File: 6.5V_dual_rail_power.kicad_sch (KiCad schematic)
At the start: 12 parts, among them U2 TSR2-2465, U3 TSR2-2465

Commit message: Save progress.
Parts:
- F1, F2: footprint (none) -> Fuse:Fuse_Littelfuse-NANO2-451_453; DigiKey Part Number (none) -> F2602TR-ND; Manufacturer (none) -> Littelfuse Inc.; Manufacturer Part Number (none) -> 0452002.MRL; Package/Footprint (none) -> 2-SMD, Square End Block; Type (none) -> SMD
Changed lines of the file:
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@@
 			)
 		)
-		(property "Footprint" ""
+		(property "Footprint" "Fuse:Fuse_Littelfuse-NANO2-451_453"
 			(at 173.99 77.978 90)
 			(hide yes)
@@
 			)
 		)
-		(property "Datasheet" ""
-			(at 173.99 76.2 0)
-			(hide yes)
-			(show_name no)
-			(do_not_autoplace no)
-			(effects
-				(font
-					(size 1.27 1.27)
-				)
-			)
-		)
-		(property "Description" "Fuse"
+		(property "Datasheet" "https://www.littelfuse.com/assetdocs/littelfuse-fuse-452-454-datasheet?assetguid=8c87aa93-80a7-4ea8-8749-a19ba03901c2"
+			(at 173.99 76.2 0)
+			(hide yes)
+			(show_name no)
+			(do_not_autoplace no)
+			(effects
+				(font
+					(size 1.27 1.27)
+				)
+			)
+		)
+		(property "Description" "FUSE BRD MNT 2A 125VAC/VDC 2SMD"
+			(at 173.99 76.2 0)
+			(hide yes)
+			(show_name no)
+			(do_not_autoplace no)
+			(effects
+				(font
+					(size 1.27 1.27)
+				)
+			)
+		)
+		(property "Manufacturer" "Littelfuse Inc."
+			(at 173.99 76.2 0)
+			(hide yes)
+			(show_name no)
+			(do_not_autoplace no)
+			(effects
+				(font
+					(size 1.27 1.27)
+				)
+			)
+		)
+		(property "Manufacturer Part Number" "0452002.MRL"
+			(at 173.99 76.2 0)
+			(hide yes)
+			(show_name no)
+			(do_not_autoplace no)
+			(effects
+				(font
+					(size 1.27 1.27)
+				)
+			)
+		)
+		(property "DigiKey Part Number" "F2602TR-ND"
+			(at 173.99 76.2 0)
+			(hide yes)
+			(show_name no)
+			(do_not_autoplace no)
+			(effects
+				(font
+					(size 1.27 1.27)
+				)
+			)
+		)
+		(property "Type" "SMD"
+			(at 173.99 76.2 0)
+			(hide yes)
+			(show_name no)
+			(do_not_autoplace no)
+			(effects
+				(font
+					(size 1.27 1.27)
+				)
+			)
+		)
+		(property "Package/Footprint" "2-SMD, Square End Block"
 			(at 173.99 76.2 0)
 			(hide yes)
@@
 			)
 		)
-		(property "Footprint" ""
+		(property "Footprint" "Fuse:Fuse_Littelfuse-NANO2-451_453"
 			(at 173.99 103.378 90)
 			(hide yes)
@@
 			)
 		)
-		(property "Datasheet" ""
-			(at 173.99 101.6 0)
-			(hide yes)
-			(show_name no)
-			(do_not_autoplace no)
-			(effects
-				(font
-					(size 1.27 1.27)
-				)
-			)
-		)
-		(property "Description" "Fuse"
-			(at 173.99 101.6 0)
-			(hide yes)
+		(property "Datasheet" "https://www.littelfuse.com/assetdocs/littelfuse-fuse-452-454-datasheet?assetguid=8c87aa93-80a7-4ea8-8749-a19ba03901c2"
+			(at 173.99 101.6 0)
+			(hide yes)
+			(show_name no)
+			(do_not_autoplace no)
+			(effects
+				(font
+					(size 1.27 1.27)
+				)
+			)
+		)
+		(property "Description" "FUSE BRD MNT 2A 125VAC/VDC 2SMD"
+			(at 173.99 101.6 0)
+			(hide yes)
+			(show_name no)
+			(do_not_autoplace no)
+			(effects
+				(font
+					(size 1.27 1.27)
+				)
+			)
+		)
+		(property "Manufacturer" "Littelfuse Inc."
+			(at 173.99 101.6 0)
+			(hide yes)
+			(show_name no)
+			(do_not_autoplace no)
+			(effects
+				(font
+					(size 1.27 1.27)
+				)
+			)
+		)
+		(property "Manufacturer Part Number" "0452002.MRL"
+			(at 173.99 101.6 0)
+			(hide yes)
+			(show_name no)
+			(do_not_autoplace no)
+			(effects
+				(font
+					(size 1.27 1.27)
+				)
+			)
+		)
+		(property "DigiKey Part Number" "F2602TR-ND"
+			(at 173.99 101.6 0)
+			(hide yes)
+			(show_name no)
+			(do_not_autoplace no)
+			(effects
+				(font
+					(size 1.27 1.27)
+				)
+			)
+		)
+		(property "Type" "SMD"
+			(at 173.99 101.6 0)
+			(hide yes)
+			(show_name no)
+			(do_not_autoplace no)
+			(effects
+				(font
+					(size 1.27 1.27)
+				)
+			)
+		)
+		(property "Package/Footprint" "2-SMD, Square End Block"
+			(at 173.99 101.6 0)
+			(hide yes)

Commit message: Save progress.
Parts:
- added C10, C11, C12, C9: 10uF, Capacitor_SMD:C_1206_3216Metric_Pad1.33x1.80mm_HandSolder, symbol DK_Murata_GRM_1206_Capacitors:C_10uF
- added L1, L2: 5.6uH, 1_L_SMD:TCK141, symbol 1_L_SMD:TCK-141
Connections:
- net +15V: now also C10.1, C9.1, L1.1; no longer C5.1, C6.1, U2.1 (Vin)
- net -15V: now also C11.2, C12.2, L2.2; no longer C7.2, C8.2, U3.2 (GND)
- net GND: now also C10.2, C11.1, C12.1, C9.2
- new net: C7.2, C8.2, L2.1, U3.2 (GND)
- new net: C5.1, C6.1, L1.2, U2.1 (Vin)

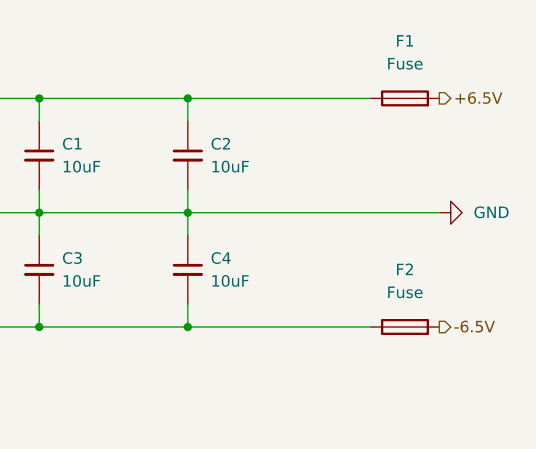
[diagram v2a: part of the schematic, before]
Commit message: Exchange SMD fuse with SMD fuse holder.
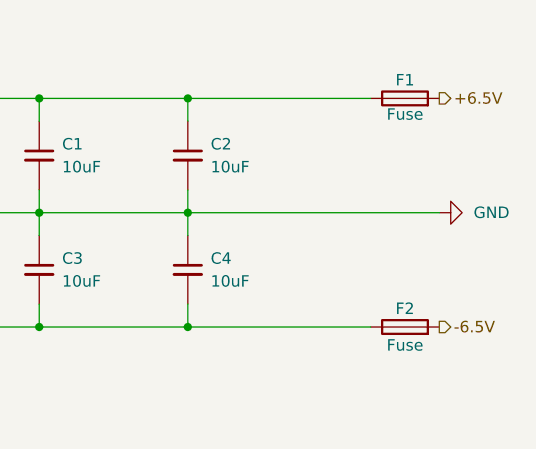
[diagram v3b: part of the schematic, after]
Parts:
- removed F1, F2: Fuse, Fuse:Fuse_Littelfuse-NANO2-451_453, symbol Device:Fuse
- added F1, F2: Fuse, 1_Fuse_SMD:LittleFuse_01550900M, symbol 1_Fuse_SMD:Littlefuse OMNI-BLOK Holder
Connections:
- net +6.5V: now also F1.2
- net -6.5V: now also F2.2
- net at C1.1, C2.1, U2.3 (Vout): now also F1.1
- net at C3.2, C4.2, U3.3 (Vout): now also F2.1

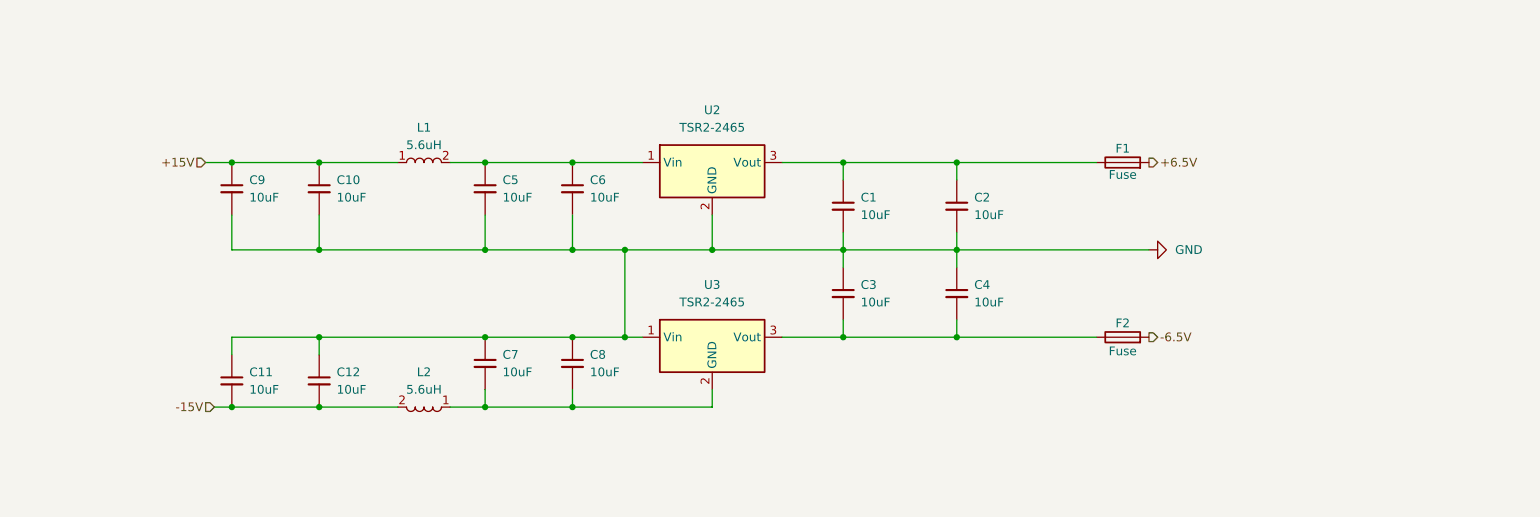
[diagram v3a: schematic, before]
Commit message: Added and routed power LEDs.
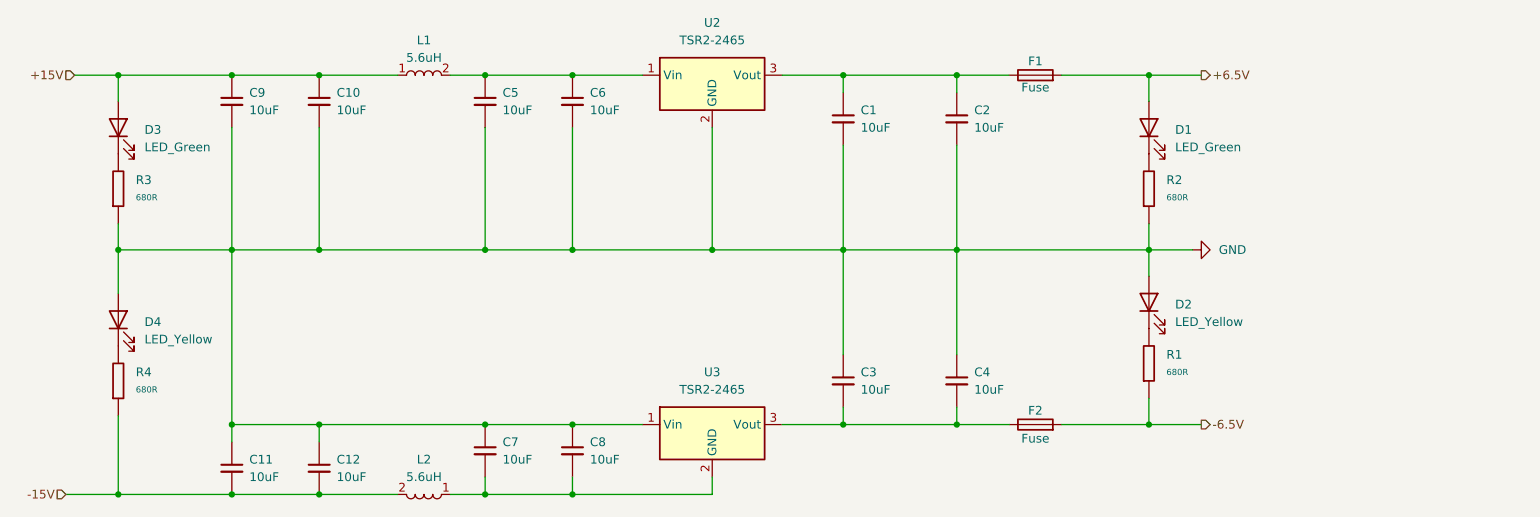
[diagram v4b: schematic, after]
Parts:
- added D1, D3: LED_Green, 1_LED_TH:LED_TH_RA, symbol 1_TH_LED:LED_Green_RA
- added D2, D4: LED_Yellow, 1_LED_TH:LED_TH_RA, symbol 1_TH_LED:LED_Yellow_RA
- added R1, R2: 680R, Resistor_SMD:R_1206_3216Metric_Pad1.30x1.75mm_HandSolder, symbol DK_Yageo_RT_1206_Resistors:R_680R
- added R3, R4: 680R, Resistor_SMD:R_1206_3216Metric_Pad1.30x1.75mm_HandSolder, symbol DK_Yageo_RT_1206_Resistors:R_1K5_4
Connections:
- net +15V: now also D3.2 (A)
- net +6.5V: now also D1.2 (A)
- net -15V: now also R4.1
- net -6.5V: now also R1.1
- net GND: now also D2.2 (A), D4.2 (A), R2.1, R3.1
- new net: D2.1 (K), R1.2
- new net: D4.1 (K), R4.2
- new net: D3.1 (K), R3.2
- new net: D1.1 (K), R2.2
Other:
- moved on the sheet: C1, C10, C11, C12, C2, C3, C4, C5, C6, C7, C8, C9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

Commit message: Added fab files.
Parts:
- D1, D2, D3, D4: Package/Footprint (none) -> LED_TH
- F1, F2: Package/Footprint (none) -> fuse_block
- L1, L2: Package/Footprint (none) -> tck_141; Type (none) -> SMD
- R3, R4: value 680R -> 1K5
- U2, U3: DigiKey Part Number (none) -> 1951-2427-ND; Manufacturer (none) -> Traco Power; Manufacturer Part Number (none) -> TSR 2-2465; Package/Footprint (none) -> 3-SIP Module; Type (none) -> thru-hole
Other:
- moved on the sheet: C1, C10, C11, C12, C2, C3, C4, C5, C6, C7, C8, C9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
